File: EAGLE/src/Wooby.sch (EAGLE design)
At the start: 29 parts, among them J1 691210910002, J2 691210910002, J3 691210910002, J4 691210910002, J5 691210910002

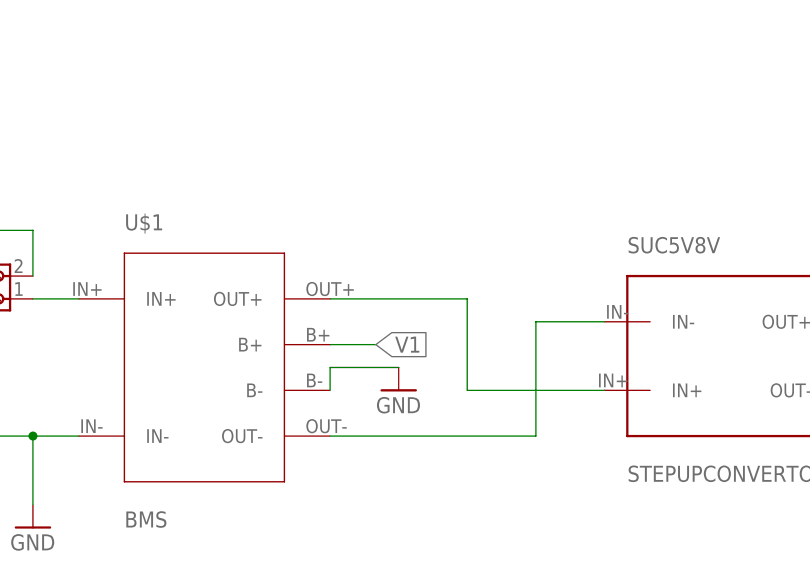
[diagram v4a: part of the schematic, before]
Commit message: ON_BTN insertion on circuit and board
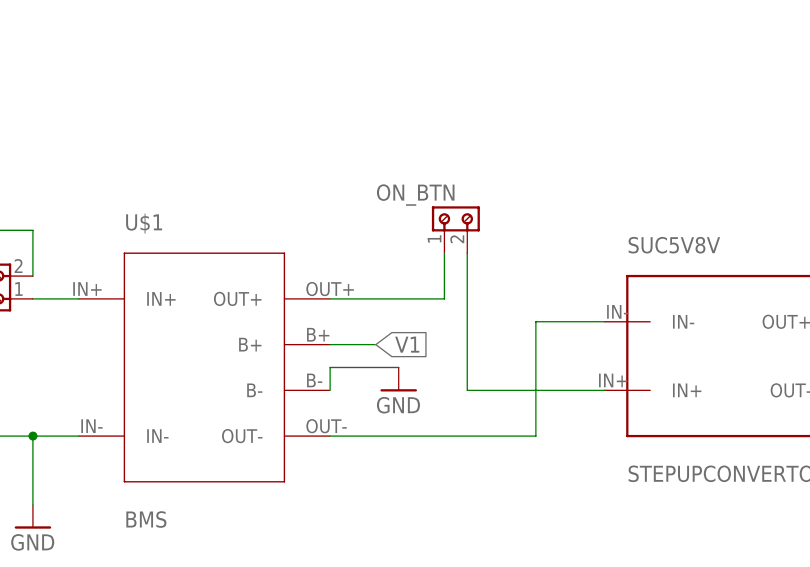
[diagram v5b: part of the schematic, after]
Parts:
- added ON_BTN: 691210910002, 691210910002:691210910002
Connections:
- new net N$52: ON_BTN.2, SUC5V8V.IN+
- net N$26: now also ON_BTN.1; no longer SUC5V8V.IN+
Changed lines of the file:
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@@
 <part name="GND15" library="supply1" library_urn="urn:adsk.eagle:library:371" deviceset="GND" device=""/>
 <part name="GND16" library="supply1" library_urn="urn:adsk.eagle:library:371" deviceset="GND" device=""/>
+<part name="ON_BTN" library="691210910002" deviceset="691210910002" device=""/>
 </parts>
 <sheets>
@@
 <instance part="GND16" gate="1" x="190.5" y="0" smashed="yes" rot="R180">
 <attribute name="VALUE" x="193.04" y="2.54" size="1.778" layer="96" rot="R180"/>
+</instance>
+<instance part="ON_BTN" gate="G$1" x="162.56" y="137.16" smashed="yes">
+<attribute name="NAME" x="152.4" y="137.922" size="1.778" layer="95"/>
 </instance>
 </instances>
@@
 <segment>
 <pinref part="U$1" gate="G$1" pin="OUT+"/>
-<wire x1="147.32" y1="127" x2="162.56" y2="127" width="0.1524" layer="91"/>
-<wire x1="162.56" y1="127" x2="162.56" y2="116.84" width="0.1524" layer="91"/>
+<pinref part="ON_BTN" gate="G$1" pin="1"/>
+<wire x1="147.32" y1="127" x2="160.02" y2="127" width="0.1524" layer="91"/>
+<wire x1="160.02" y1="127" x2="160.02" y2="132.08" width="0.1524" layer="91"/>
+</segment>
+</net>
+<net name="N$52" class="0">
+<segment>
+<pinref part="ON_BTN" gate="G$1" pin="2"/>
+<wire x1="162.56" y1="132.08" x2="162.56" y2="116.84" width="0.1524" layer="91"/>
 <pinref part="SUC5V8V" gate="G$1" pin="IN+"/>
 <wire x1="162.56" y1="116.84" x2="177.8" y2="116.84" width="0.1524" layer="91"/>

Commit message: Lady D Version
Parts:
- removed CELL, CELL1, CELL2, CELL3, J1, J2, J3, J4, J5: 691210910002, 691210910002:691210910002
- added SV1, SV2, SV3, SV4: (no value), con-lstb:MA04-1
- LCD: value 691210910002 -> (none); device 691210910002:691210910002 -> con-lstb:MA04-1
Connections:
- net +3V3: now also LCD.3; no longer LCD.1
- net GND: now also LCD.4; no longer LCD.2
- net N$1: now also SV1.3; no longer CELL.1
- net N$13: now also SV4.4; no longer CELL3.2
- net N$14: now also SV4.3; no longer CELL3.1
- net N$15: now also SV4.2; no longer J4.2
- net N$16: now also SV4.1; no longer J4.1
- net N$17: now also SV3.4; no longer CELL2.2
- net N$18: now also SV3.3; no longer CELL2.1
- net N$19: now also SV3.2; no longer J3.2
- net N$2: now also SV1.4; no longer CELL.2
- net N$20: now also SV3.1; no longer J3.1
- net N$21: now also SV2.4; no longer CELL1.2
- net N$22: now also SV2.3; no longer CELL1.1
- net N$23: now also SV2.2; no longer J1.2
- net N$24: now also SV2.1; no longer J1.1
- net N$3: now also SV1.1; no longer J5.1
- net N$4: now also SV1.2; no longer J5.2
- net N$6: now also LCD.2; no longer J2.2
- net N$7: now also LCD.1; no longer J2.1
